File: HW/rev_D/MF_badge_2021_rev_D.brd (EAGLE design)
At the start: 61 x 100.5 mm, 165 parts, among them IC1 MCP73831, J1 HRO_31_M_12_USB_C, Q1 SI1308EDL-T1-GE3, Q2 DMG3415U-7, Q3 DMG3415U-7, Q4 DMG3415U-7, U1 ESP32-S2-WROOM, U2 AP2112K-3.3, X1 CAPTOUCH_10MM, X2 CAPTOUCH_10MM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

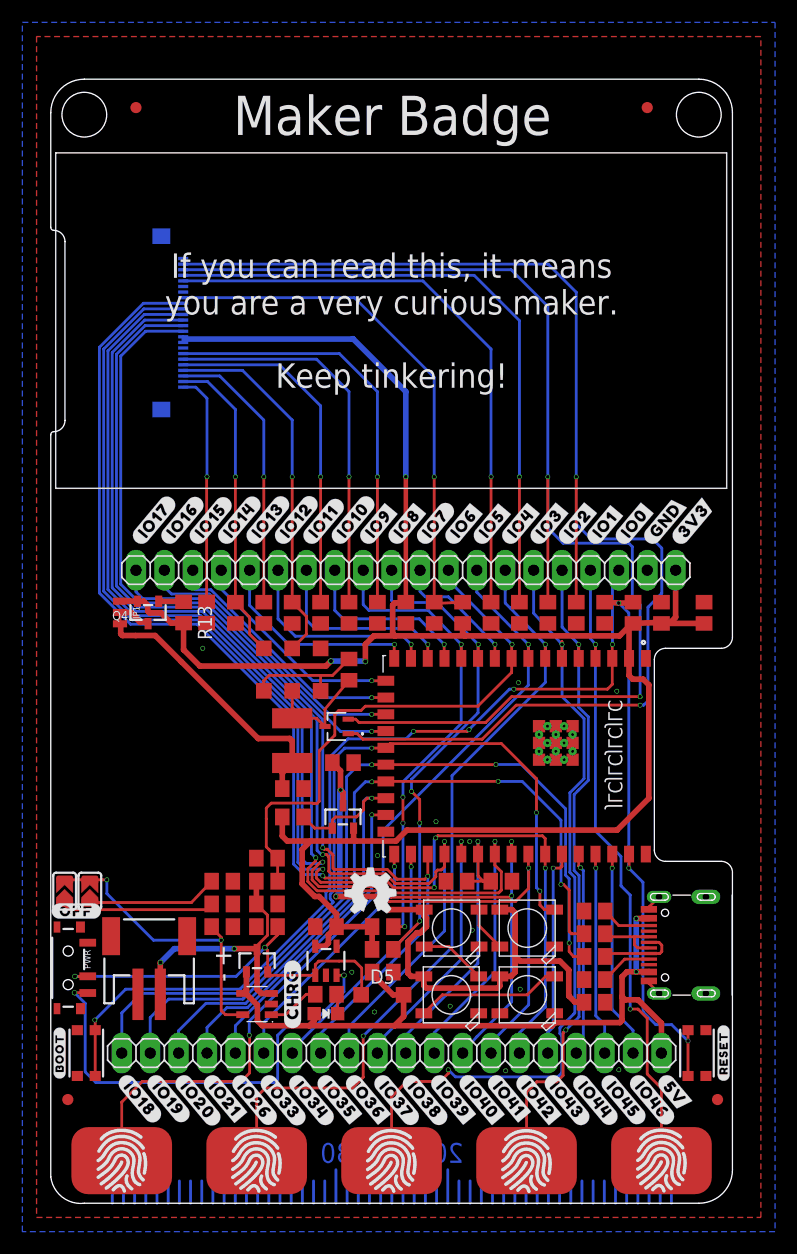
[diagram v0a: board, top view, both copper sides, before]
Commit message: Update
- removed CR2032 battery holder
- changed battery measuring circuit to save power
- add N-MOSFET to control 3V3 to e-ink displey
- changed QR to match new project address
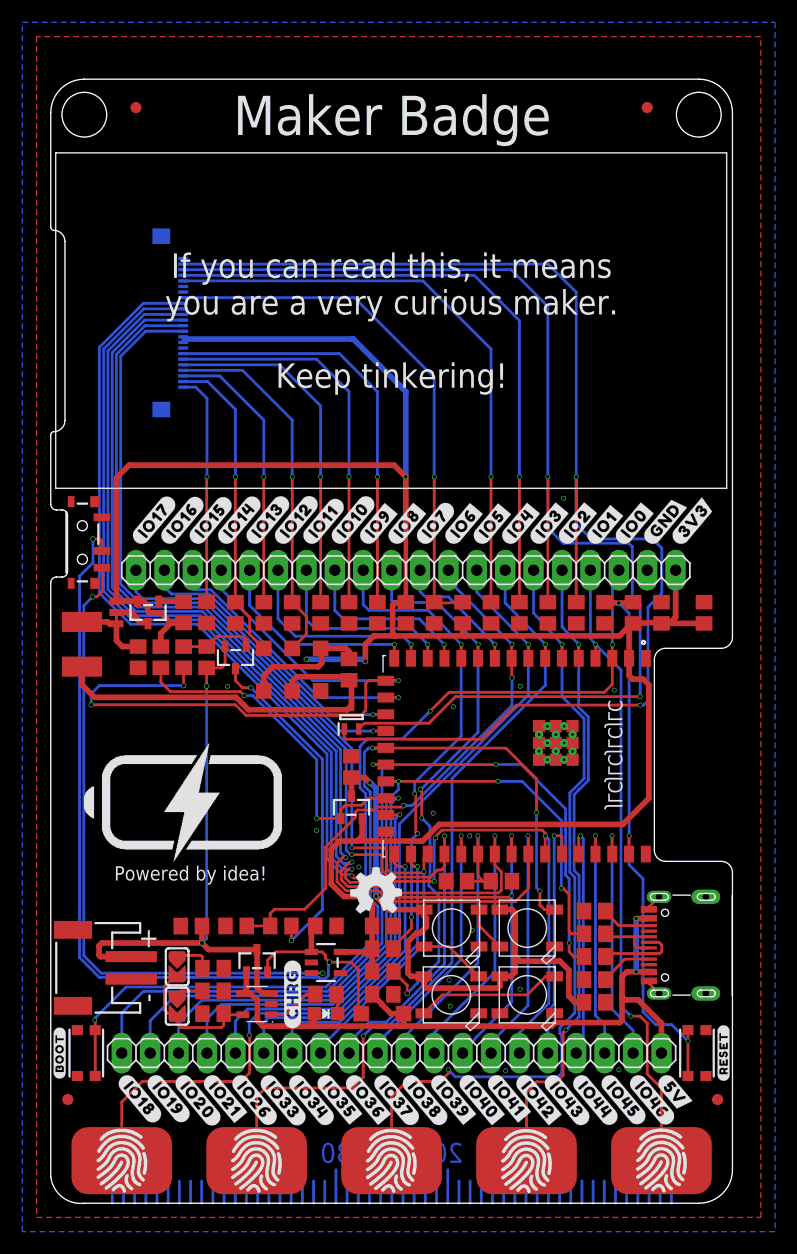
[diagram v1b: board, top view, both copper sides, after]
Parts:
- removed Q1: SI1308EDL-T1-GE3, SI1308EDL-T1-GE3:MOSFET_8EDL-T1-GE3_VIS
- removed U$56: (no value), output:#OFF#0
- added C21: 100n, rcl:C0805
- added Q5: Si2305, microbuilder:SOT23-R
- added Q6: SI1308EDL-T1-GE3, SamacSys_Parts:SOT65P210X110-3N
- added R14: 10k, rcl:R0805
- moved PWR 38.1 mm to (2.83, 59.1)
- moved L1 20.7 mm to (2.79, 50.0), turned to 270 degrees
- moved R5 18.5 mm to (9.84, 48.8), turned to 90 degrees
- moved C12 18.2 mm to (7.81, 48.8), turned to 270 degrees
- moved RATE2 14.4 mm to (11.3, 17.6), turned to 270 degrees
- moved RATE1 10.3 mm to (11.3, 21.1), turned to 270 degrees
- moved R7 7.82 mm to (14.5, 17.0), turned to 180 degrees
- moved R11 7.82 mm to (14.5, 21.0)
- moved R12 7.82 mm to (14.5, 19.0)
- moved C13 7.05 mm to (12.6, 24.8), turned to 180 degrees
- moved R31 6.66 mm to (16.6, 24.8)
- moved U$8 5.47 mm to (3.49, 21.1), turned to 90 degrees
- moved C14 5.27 mm to (24.6, 24.8), turned to 0 degrees
- moved C20 5.08 mm to (29.7, 24.8), turned to 0 degrees
- moved R30 4.19 mm to (20.6, 24.8), turned to 0 degrees
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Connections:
- new net N$79: Q5.3, R30.2
- new net N$80: C21.1, Q5.1, R14.1
- net BAT+: now also Q5.2, R14.2; no longer R30.2
- net IO14: now also C21.2
- net N$10: now also Q6.2; no longer Q1.2
- net N$13: now also Q6.1; no longer Q1.1
- net N$19: now also Q6.3; no longer Q1.3
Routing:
- net N$9: track 36.1 -> 81.0 mm
- net IO14: track 19.8 -> 62.6 mm, vias 1 -> 3
- net N$79: track 0.00 -> 30.4 mm, vias 0 -> 2
- net BAT+: track 24.0 -> 53.1 mm
- net IO21: track 40.0 -> 67.7 mm, vias 1 -> 3
- net N$19: track 10.6 -> 35.4 mm
- net +3V3: track 183.0 -> 203.3 mm
- net N$18: track 40.0 -> 58.7 mm
- net N$26: track 24.8 -> 6.70 mm
- net PROG: track 26.9 -> 12.7 mm, vias 2 -> 0
- net N$21: track 13.8 -> 2.40 mm
- net N$20: track 11.7 -> 3.32 mm
- net IO8_SDA: track 44.5 -> 51.2 mm
- net N$80: track 0.00 -> 6.68 mm
- net IO26: track 27.6 -> 33.2 mm
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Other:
- outline, holes or cut-outs redrawn
- board text added: "Based on idea by Luboš Moravec (@Bastlir)"
- board text added: "More info & code examples"
- board text added: "Powered by idea!"
- board text added: "github.com/ makerfaireczech/ maker_badge"
- board text removed: "Based on idea by twitch.tv/bastlir"
- board text removed: "More info, code examples"
- board text removed: "doresit label pro IO19 & IO20 -> USB piny"
- board text removed: "github.com/dronecz/ maker_badge"

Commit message: Update
- schematic cleanup
- power supply layout optimization
- changed some R and C values
- add hole for battery holder
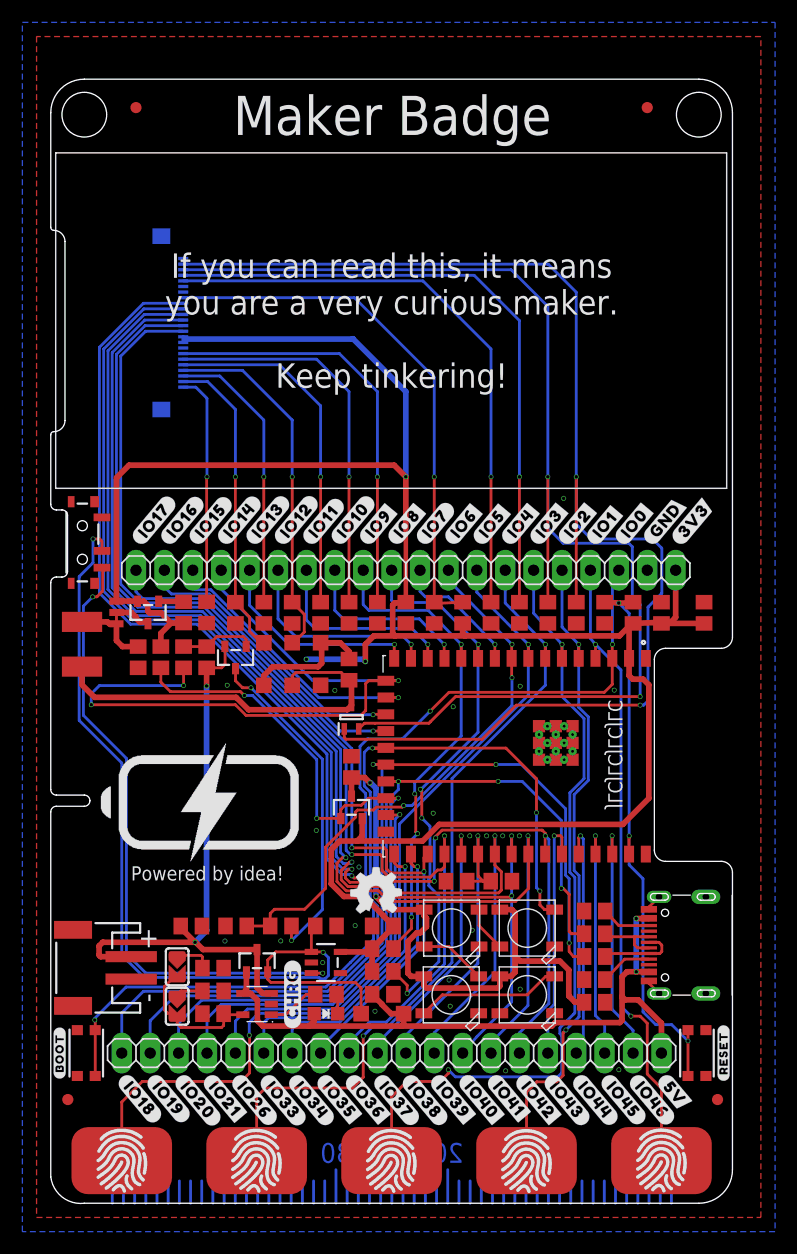
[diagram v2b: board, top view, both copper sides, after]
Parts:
- C10, C12: value 4u7 -> 4u7F
- C13, C14, C16, C19, C20: value 10u -> 10uF
- C15, C17, C22, C9: value 1u -> 1uF
- C18: value 100n -> 10uF
- C21, C8: value 100n -> 100nF
- R1, R10, R11, R12, R14, R30, R31, R7, R8: value 10k -> 10K
- R13, R5: value 100k -> 10K
- R15, R16: value 5k1 -> 5K1
- R17, R18: value 22 -> 22R
- R2: value 0.47 -> 0.47R
- R22, R23: value 4k7 -> 4K7
- R6: value 1k -> 1K
- moved D1 0.50 mm to (21.6, 48.2)
- moved D2 0.50 mm to (19.1, 48.2)
- moved D3 0.50 mm to (24.1, 48.2)
- turned C13 to 0 degrees
- turned C20 to 180 degrees
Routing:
- net N$18: track 58.7 -> 56.4 mm
- net N$9: track 81.0 -> 83.2 mm
- net +3V3: track 203.3 -> 204.8 mm
- net BAT+: track 53.1 -> 53.7 mm
- net N$4: track 33.1 -> 32.5 mm
- net GND: vias 15 -> 24
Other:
- outline, holes or cut-outs redrawn

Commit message: Update
- bigger slot for battery holder
- GND stitching for better RF
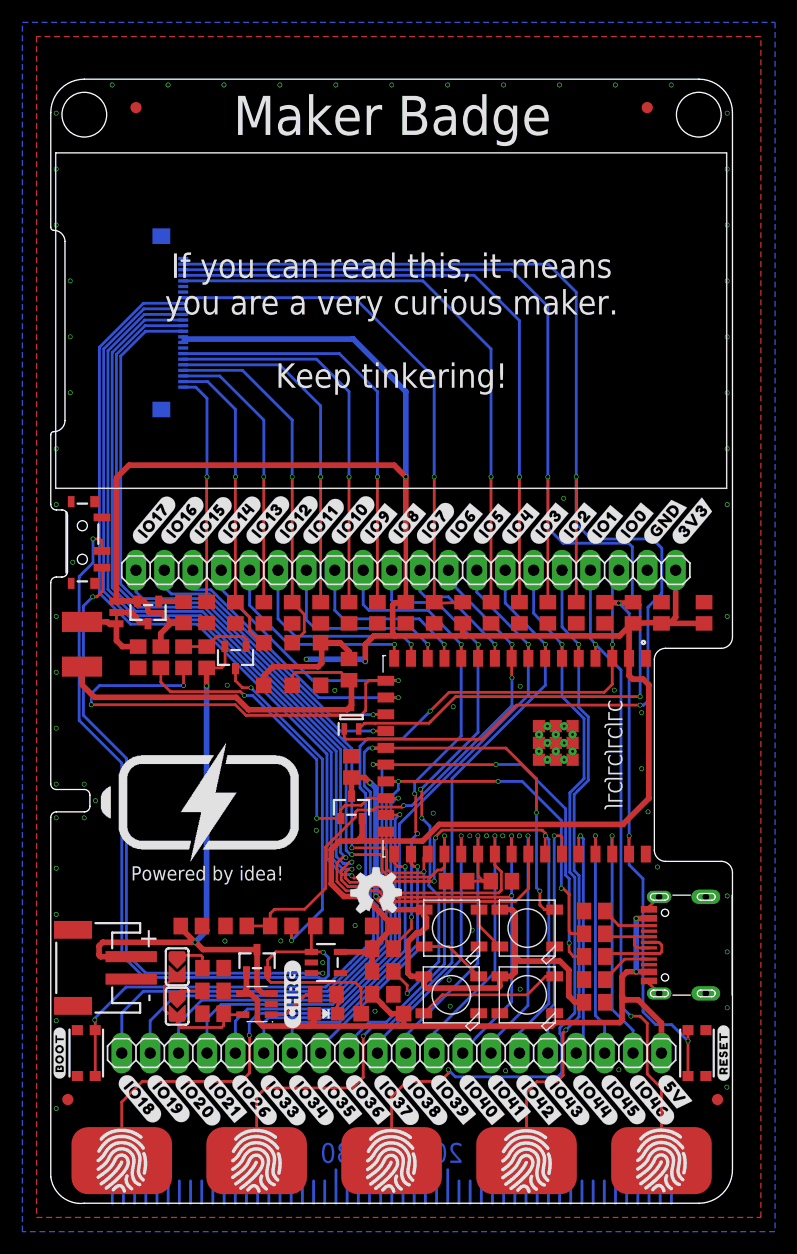
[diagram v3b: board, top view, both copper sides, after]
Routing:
- net GND: vias 24 -> 73
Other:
- outline, holes or cut-outs redrawn
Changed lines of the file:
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@@
 <layer number="39" name="tKeepout" color="4" fill="11" visible="yes" active="yes"/>
 <layer number="40" name="bKeepout" color="1" fill="11" visible="yes" active="yes"/>
-<layer number="41" name="tRestrict" color="4" fill="10" visible="no" active="yes"/>
-<layer number="42" name="bRestrict" color="1" fill="10" visible="no" active="yes"/>
+<layer number="41" name="tRestrict" color="4" fill="10" visible="yes" active="yes"/>
+<layer number="42" name="bRestrict" color="1" fill="10" visible="yes" active="yes"/>
 <layer number="43" name="vRestrict" color="2" fill="10" visible="no" active="yes"/>
 <layer number="44" name="Drills" color="7" fill="1" visible="no" active="yes"/>
@@
 </layers>
 <board>
-<fusionsync huburn="a.cGVyc29uYWw6dWUyOTJiMTg5" projecturn="a.cGVyc29uYWw6dWUyOTJiMTg5IzIwMTYwODEyMzk2NDM1NTY" f3durn="urn:adsk.wipprod:dm.lineage:CPsKkGpEQ_-sErX5hWt2dw" pcbguid="423eee16-d896-4c93-8b5f-76290c7fc869" lastpulledtime="" lastsyncedchangeguid="" latestrevisionid="95d10fbb-f0ee-4243-9bcb-40a1d4a13679" lastsyncedrevisionid="95d10fbb-f0ee-4243-9bcb-40a1d4a13679" lastboardhashguid="fc95ef11-20e9-6119-56d4-9a92fcbb6dbc" lastpushedtime="2023-03-02T23:16:09Z" linktopcb3d="true"/>
+<fusionsync huburn="a.cGVyc29uYWw6dWUyOTJiMTg5" projecturn="a.cGVyc29uYWw6dWUyOTJiMTg5IzIwMTYwODEyMzk2NDM1NTY" f3durn="urn:adsk.wipprod:dm.lineage:CPsKkGpEQ_-sErX5hWt2dw" pcbguid="" lastpulledtime="" lastsyncedchangeguid="" latestrevisionid="95d10fbb-f0ee-4243-9bcb-40a1d4a13679" lastsyncedrevisionid="95d10fbb-f0ee-4243-9bcb-40a1d4a13679" lastboardhashguid="fc95ef11-20e9-6119-56d4-9a92fcbb6dbc" lastpushedtime="2023-03-02T23:16:09Z" linktopcb3d="true"/>
 <plain>
 <hole x="57.95" y="97.345" drill="4"/>
@@
 <wire x1="0" y1="87.27" x2="0.27" y2="87" width="0.0762" layer="20" curve="90"/>
 <wire x1="0" y1="97.52" x2="3" y2="100.52" width="0.0762" layer="20" curve="-90"/>
-<wire x1="0" y1="2.365" x2="0" y2="35" width="0.0762" layer="20"/>
-<wire x1="0" y1="35" x2="0.5" y2="35.5" width="0.0762" layer="20" curve="-90"/>
-<wire x1="0.5" y1="35.5" x2="3" y2="35.5" width="0.0762" layer="20"/>
-<wire x1="3" y1="35.5" x2="3.5" y2="36" width="0.0762" layer="20" curve="90"/>
-<wire x1="3.5" y1="36" x2="3" y2="36.5" width="0.0762" layer="20" curve="90"/>
-<wire x1="3" y1="36.5" x2="0.5" y2="36.5" width="0.0762" layer="20"/>
-<wire x1="0.5" y1="36.5" x2="0" y2="37" width="0.0762" layer="20" curve="-90"/>
-<wire x1="0" y1="37" x2="0" y2="55.5" width="0.0762" layer="20"/>
+<wire x1="3" y1="35" x2="0.5" y2="35" width="0.0762" layer="20"/>
+<wire x1="0.5" y1="35" x2="0" y2="34.5" width="0.0762" layer="20" curve="90"/>
+<wire x1="0" y1="34.5" x2="0" y2="2.365" width="0.0762" layer="20"/>
+<wire x1="3.5" y1="36.5" x2="3.5" y2="35.5" width="0.0762" layer="20"/>
+<wire x1="3.5" y1="35.5" x2="3" y2="35" width="0.0762" layer="20" curve="-90"/>
+<wire x1="0.5" y1="37" x2="3" y2="37" width="0.0762" layer="20"/>
+<wire x1="3" y1="37" x2="3.5" y2="36.5" width="0.0762" layer="20" curve="-90"/>
+<wire x1="0.5" y1="37" x2="0" y2="37.5" width="0.0762" layer="20" curve="-90"/>
+<wire x1="0" y1="37.5" x2="0" y2="55.5" width="0.0762" layer="20"/>
 <wire x1="0" y1="55.5" x2="0.5" y2="56" width="0.0762" layer="20" curve="-90"/>
 <wire x1="0.5" y1="56" x2="1" y2="56" width="0.0762" layer="20"/>
@@
 <via x="28.9925" y="17.174" extent="1-16" drill="0.3"/>
 <via x="25.402" y="45.8605" extent="1-16" drill="0.3"/>
+<via x="0.489" y="8.4735" extent="1-16" drill="0.3"/>
+<via x="0.489" y="16.32475" extent="1-16" drill="0.3"/>
+<via x="0.489" y="25.828" extent="1-16" drill="0.3"/>
+<via x="0.489" y="29.9555" extent="1-16" drill="0.3"/>
+<via x="0.489" y="34.464" extent="1-16" drill="0.3"/>
+<via x="0.489" y="37.479" extent="1-16" drill="0.3"/>
+<via x="0.489" y="42.479" extent="1-16" drill="0.3"/>
+<via x="0.489" y="47.479" extent="1-16" drill="0.3"/>
+<via x="0.489" y="52.479" extent="1-16" drill="0.3"/>
+<via x="1.96525" y="57.32025" extent="1-16" drill="0.3"/>
+<via x="0.489" y="62.479" extent="1-16" drill="0.3"/>
+<via x="0.489" y="67.479" extent="1-16" drill="0.3"/>
+<via x="1.743" y="72.479" extent="1-16" drill="0.3"/>
+<via x="1.743" y="77.479" extent="1-16" drill="0.3"/>
+<via x="1.743" y="82.479" extent="1-16" drill="0.3"/>
+<via x="0.489" y="87.479" extent="1-16" drill="0.3"/>
+<via x="0.489" y="92.479" extent="1-16" drill="0.3"/>
+<via x="0.489" y="97.479" extent="1-16" drill="0.3"/>
+<via x="5.489" y="100.0025" extent="1-16" drill="0.3"/>
+<via x="10.489" y="100.0025" extent="1-16" drill="0.3"/>
+<via x="15.489" y="100.0025" extent="1-16" drill="0.3"/>
+<via x="20.489" y="100.0025" extent="1-16" drill="0.3"/>
+<via x="25.489" y="100.0025" extent="1-16" drill="0.3"/>
+<via x="30.489" y="100.0025" extent="1-16" drill="0.3"/>
+<via x="35.489" y="100.0025" extent="1-16" drill="0.3"/>
+<via x="40.489" y="100.0025" extent="1-16" drill="0.3"/>
+<via x="45.489" y="100.0025" extent="1-16" drill="0.3"/>
+<via x="50.489" y="100.0025" extent="1-16" drill="0.3"/>
+<via x="55.489" y="100.0025" extent="1-16" drill="0.3"/>
+<via x="60.489" y="97.479" extent="1-16" drill="0.3"/>
+<via x="60.489" y="92.479" extent="1-16" drill="0.3"/>
+<via x="60.489" y="82.479" extent="1-16" drill="0.3"/>
+<via x="60.489" y="87.479" extent="1-16" drill="0.3"/>
+<via x="60.489" y="77.479" extent="1-16" drill="0.3"/>
+<via x="60.489" y="72.479" extent="1-16" drill="0.3"/>
+<via x="60.489" y="67.479" extent="1-16" drill="0.3"/>
+<via x="60.489" y="62.479" extent="1-16" drill="0.3"/>
+<via x="60.489" y="52.479" extent="1-16" drill="0.3"/>
+<via x="52.8385" y="43.876" extent="1-16" drill="0.3"/>
+<via x="53.41" y="35.0025" extent="1-16" drill="0.3"/>
+<via x="52.8385" y="38.8595" extent="1-16" drill="0.3"/>
+<via x="54.25075" y="30.066" extent="1-16" drill="0.3"/>
+<via x="60.489" y="27.479" extent="1-16" drill="0.3"/>
+<via x="60.489" y="22.479" extent="1-16" drill="0.3"/>
+<via x="60.489" y="17.479" extent="1-16" drill="0.3"/>
+<via x="60.45725" y="10.3835" extent="1-16" drill="0.3"/>
+<via x="2.989" y="37.479" extent="1-16" drill="0.3"/>
+<via x="2.989" y="34.464" extent="1-16" drill="0.3"/>
+<via x="4" y="36" extent="1-16" drill="0.3"/>
 </signal>
 <signal name="N$16">
